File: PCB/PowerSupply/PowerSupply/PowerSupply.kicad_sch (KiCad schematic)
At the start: 18 parts

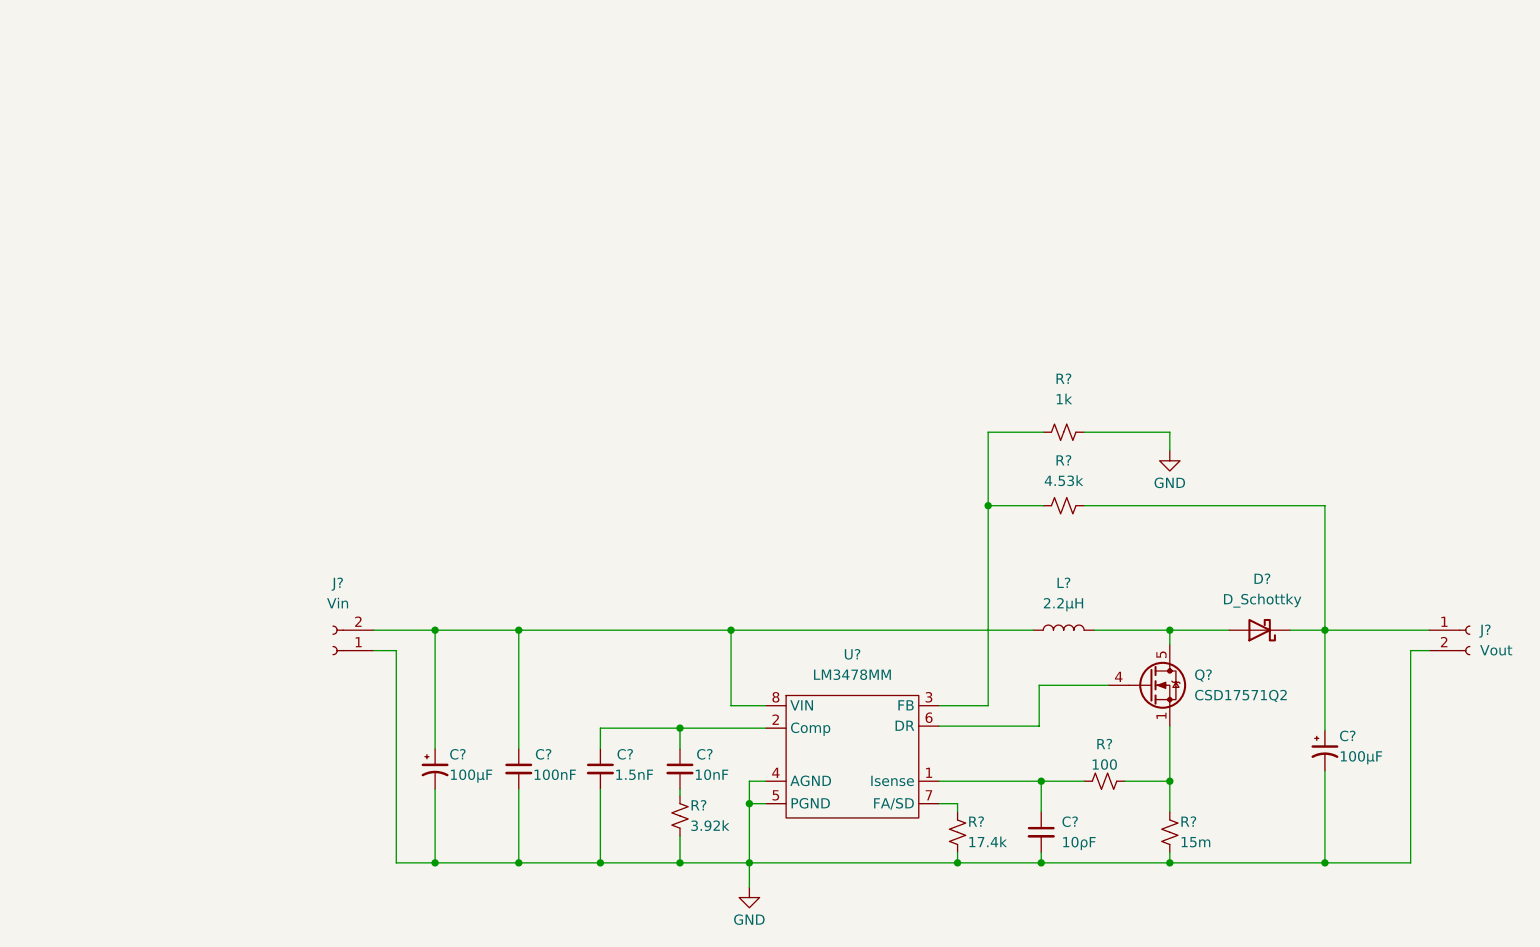
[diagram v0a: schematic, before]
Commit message: Added datasheet + Kicad modif
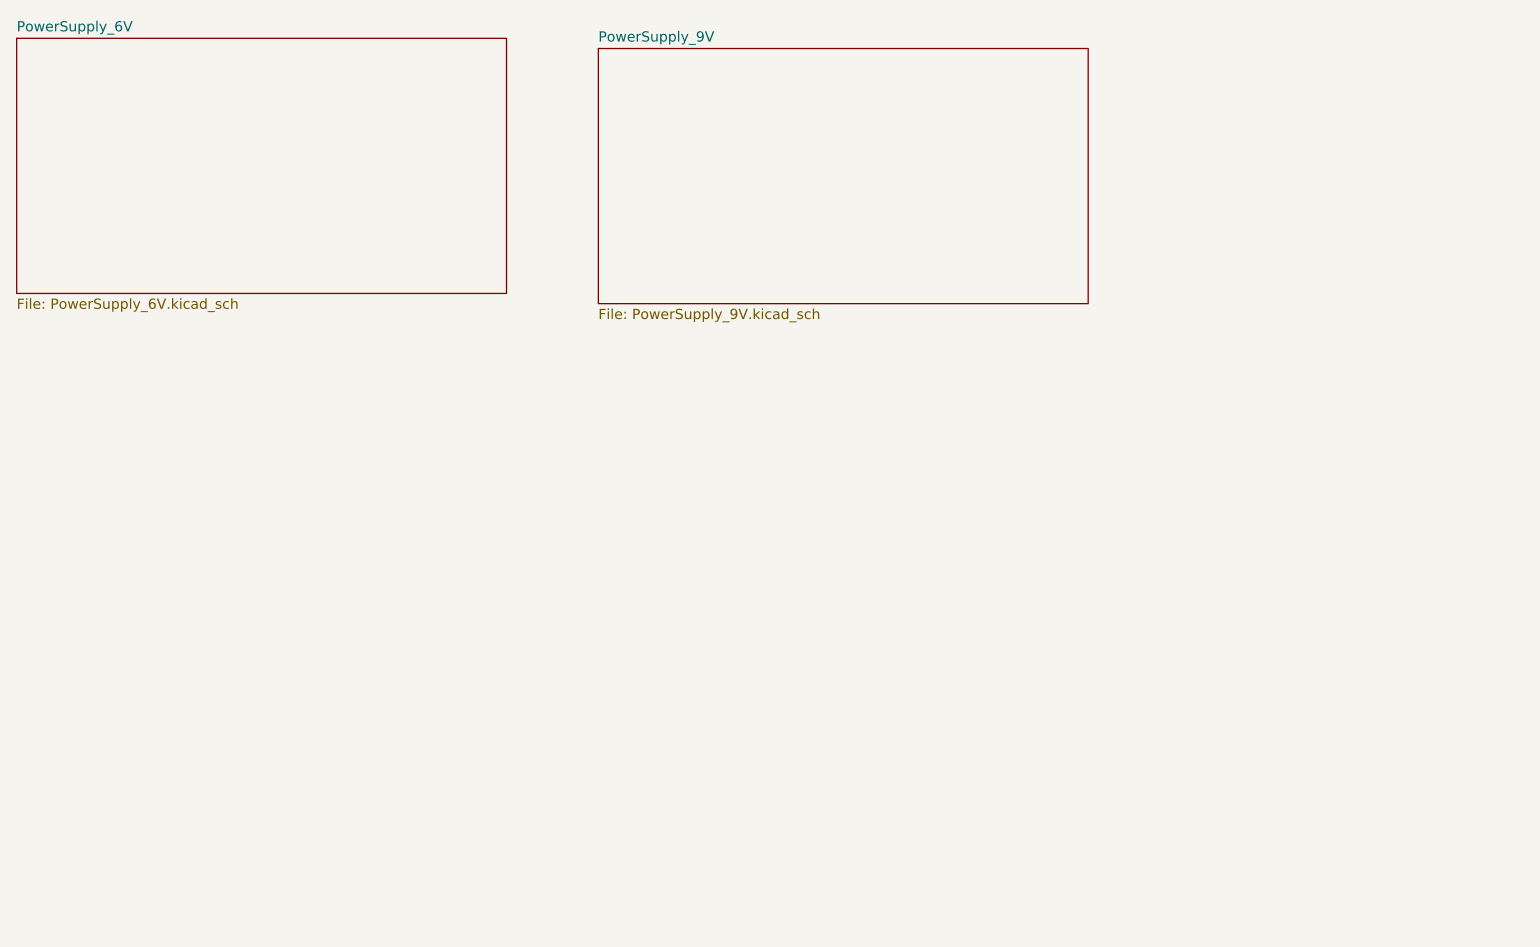
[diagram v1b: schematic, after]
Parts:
- removed C?: 1.5nF, Capacitor_SMD:C_0805_2012Metric_Pad1.18x1.45mm_HandSolder, symbol Device:C_Small
- removed C?: 100nF, Capacitor_SMD:C_0402_1005Metric_Pad0.74x0.62mm_HandSolder, symbol Device:C_Small
- removed C?: 100µF, Capacitor_SMD:C_0805_2012Metric_Pad1.18x1.45mm_HandSolder, symbol Device:C_Polarized_Small_US
- removed C?: 10nF, Resistor_SMD:R_0402_1005Metric_Pad0.72x0.64mm_HandSolder, symbol Device:C_Small
- removed C?: 100µF, Capacitor_SMD:CP_Elec_10x10, symbol Device:C_Polarized_Small_US
- removed C?: 10ρF, Capacitor_SMD:C_0805_2012Metric_Pad1.18x1.45mm_HandSolder, symbol Device:C_Small
- removed D?: D_Schottky, Diode_SMD:D_SMB-SMC_Universal_Handsoldering, symbol Device:D_Schottky
- removed J?: Vin, Connector_PinHeader_2.54mm:PinHeader_1x02_P2.54mm_Vertical, symbol Connector:Conn_01x02_Female
- removed J?: Vout, Connector_PinHeader_2.54mm:PinHeader_1x02_P2.54mm_Vertical, symbol Connector:Conn_01x02_Female
- removed L?: 2.2µH, Inductor_SMD:L_TDK_VLP8040, symbol Device:L
- removed Q?: CSD17571Q2, Package_SON:Texas_DQK, symbol Transistor_FET:CSD17579Q5A
- removed R?: 3.92k, Resistor_SMD:R_0805_2012Metric_Pad1.20x1.40mm_HandSolder, symbol Device:R_Small_US
- removed R?: 15m, Resistor_SMD:R_1206_3216Metric_Pad1.30x1.75mm_HandSolder, symbol Device:R_Small_US
- removed R?: 4.53k, Resistor_SMD:R_0402_1005Metric_Pad0.72x0.64mm_HandSolder, symbol Device:R_Small_US
- removed R?: 100, Resistor_SMD:R_0805_2012Metric_Pad1.20x1.40mm_HandSolder, symbol Device:R_Small_US
- removed R?: 17.4k, Resistor_SMD:R_0402_1005Metric_Pad0.72x0.64mm_HandSolder, symbol Device:R_Small_US
- removed R?: 1k, Resistor_SMD:R_0402_1005Metric_Pad0.72x0.64mm_HandSolder, symbol Device:R_Small_US
- removed U?: LM3478MM, Package_SO:SOIC-8-1EP_3.9x4.9mm_P1.27mm_EP2.29x3mm, symbol CustomPower:LM3478MM
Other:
- added sheet PowerSupply_6V (PowerSupply_6V.kicad_sch)
- added sheet PowerSupply_9V (PowerSupply_9V.kicad_sch)

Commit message: Finished v0.1
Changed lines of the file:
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@@
     )
   )
-  (sheet (at 25.4 16.51) (size 60.96 31.75) (fields_autoplaced)
+  (sheet (at 25.4 17.78) (size 60.96 31.75) (fields_autoplaced)
     (stroke (width 0.1524) (type solid) (color 0 0 0 0))
     (fill (color 0 0 0 0.0000))
-    (property "Sheet name" "PowerSupply_6V" (id 0) (at 25.4 15.7984 0)
+    (property "Sheet name" "PowerSupply_6V" (id 0) (at 25.4 17.0684 0)
       (effects (font (size 1.27 1.27)) (justify left bottom))
     )
-    (property "Sheet file" "PowerSupply_6V.kicad_sch" (id 1) (at 25.4 48.8446 0)
+    (property "Sheet file" "PowerSupply_6V.kicad_sch" (id 1) (at 25.4 50.1146 0)
       (effects (font (size 1.27 1.27)) (justify left top))
     )
@@
   )
   (symbol_instances
+    (path "/d52e6e97-797a-47f3-9e84-2594d0785aa0/66d410c0-7cfb-449e-9a14-33526c090e49"
+      (reference "#FLG0101") (unit 1) (value "PWR_FLAG") (footprint "")
+    )
     (path "/d52e6e97-797a-47f3-9e84-2594d0785aa0/a6cca68e-2819-49c2-af51-6d2a54e1615b"
       (reference "#PWR0101") (unit 1) (value "GND") (footprint "")
@@
       (reference "#PWR0104") (unit 1) (value "GND") (footprint "")
     )
+    (path "/d52e6e97-797a-47f3-9e84-2594d0785aa0/eb233b0f-a872-4930-aedf-8c6d215fd56e"
+      (reference "#PWR0105") (unit 1) (value "GND") (footprint "")
+    )
     (path "/d52e6e97-797a-47f3-9e84-2594d0785aa0/408f320a-98fc-43da-b743-5ca46a73fedb"
